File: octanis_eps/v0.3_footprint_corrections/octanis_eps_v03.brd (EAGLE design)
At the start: 61.9 x 49.5 mm, 100 parts, among them IC1 OPA2333DGK, IC5 OPA2333DGK, IC7 OPA2333DGK, IC9 OPA2333DGK, Q1 FC-12M, Q2 N-HEXFET-2D_SOT232-, Q3 N-HEXFET-2D_SOT232-, Q4 N-HEXFET-2D_SOT232-

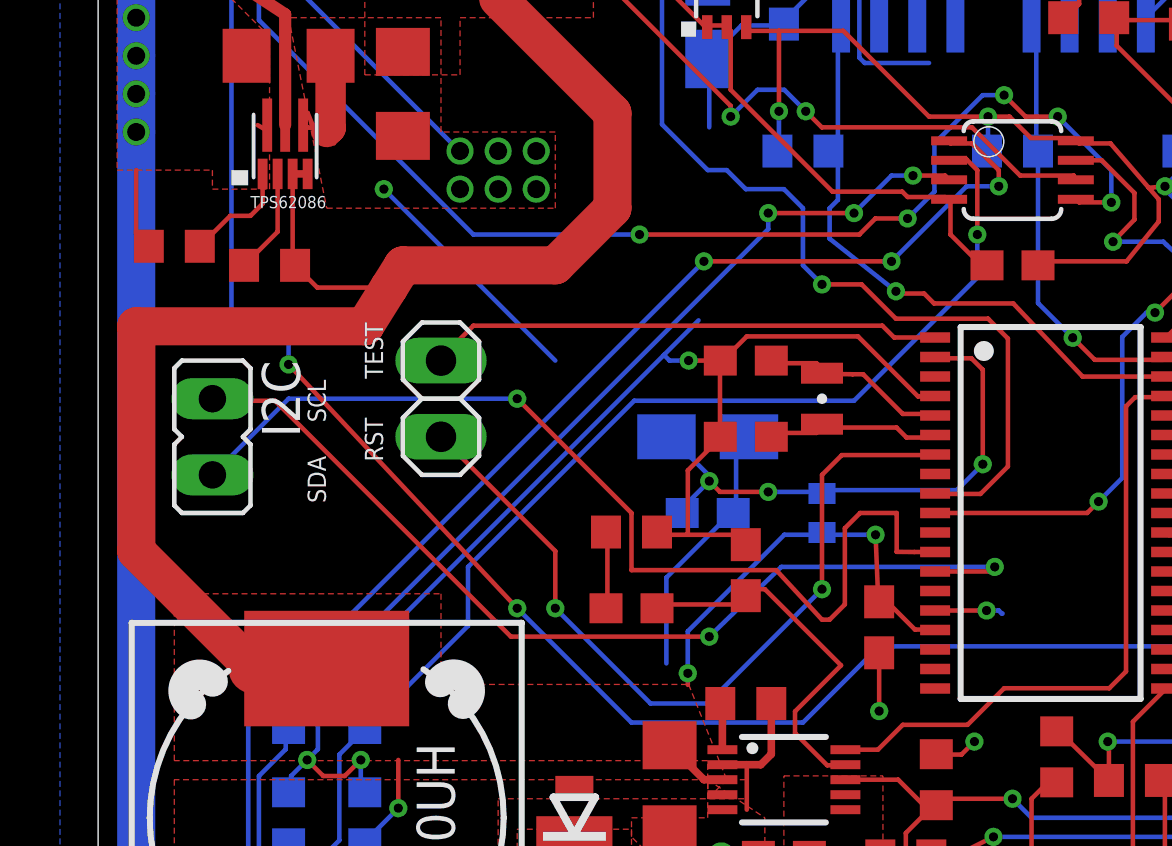
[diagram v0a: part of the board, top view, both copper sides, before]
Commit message: pull-up on RST, need to modify the current sensor pads
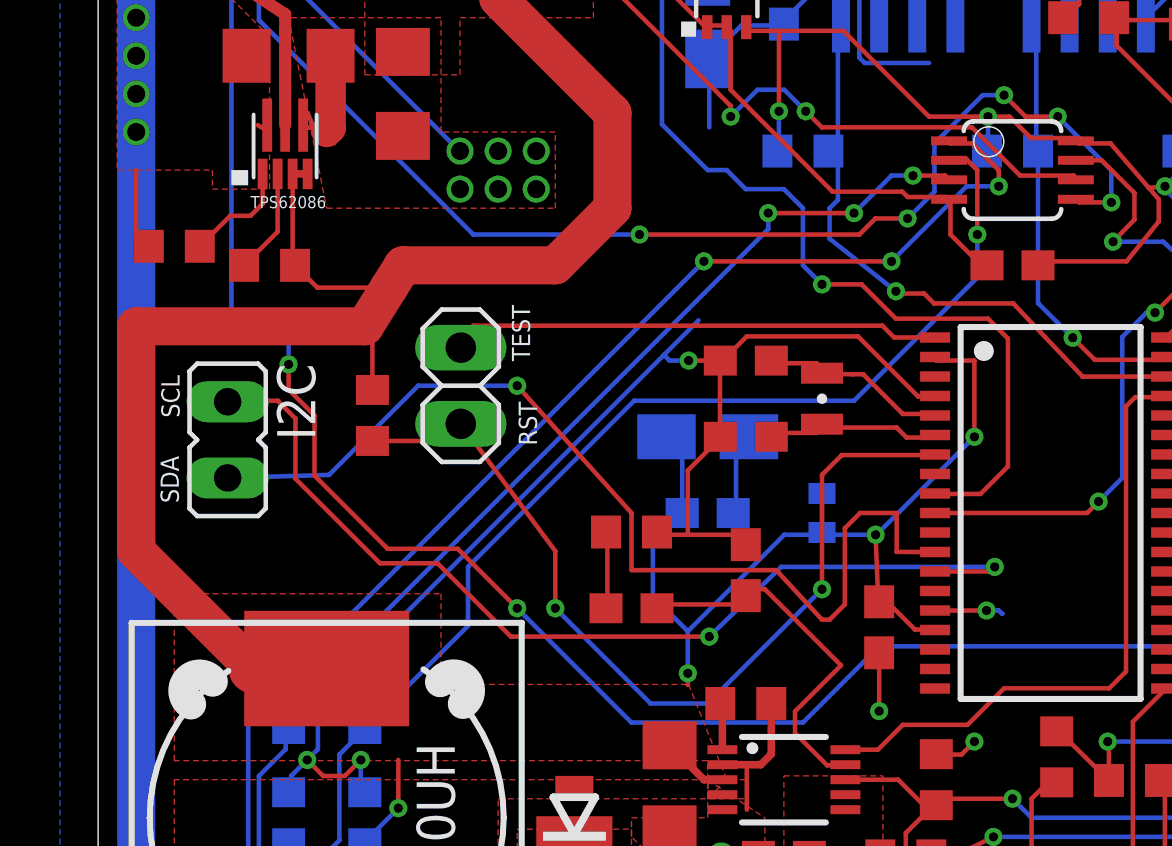
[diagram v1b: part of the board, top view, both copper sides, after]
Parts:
- added R46: 10k, rcl:R0603
- moved JP7 0.79 mm to (12.1, 52.5)
- moved I2C 0.52 mm to (4.32, 50.7)
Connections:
- removed net +3V3: C22.1, C24.+, FERRITE_BEAD.1, U$6.2
- net RST/SBWTDIO: now also R46.2
- net VCC: now also C22.1, C24.+, FERRITE_BEAD.1, R46.1, U$6.2
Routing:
- net VCC: track 341.7 -> 361.4 mm, vias 14 -> 15
- net +3V3: track 18.2 -> 0.00 mm, vias 3 -> 0
- net GND: track 275.1 -> 261.2 mm, vias 29 -> 28
- net RST/SBWTDIO: track 26.9 -> 30.0 mm
- net N$10: track 95.2 -> 96.7 mm
- net TEST/SBWTCK: track 17.2 -> 16.4 mm
- net I2C_SCL: track 32.3 -> 33.1 mm
